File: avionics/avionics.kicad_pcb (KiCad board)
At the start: 4 copper layers, 103 x 60 mm, 68 parts, among them J1 BAT Balancing leads, J2 BAT, J3 PYRO_0, J4 Servo_0, J5 Servo_1, J6 Servo_2, J7 Servo_3, Q1 AO3400A, Q2 AO3401A, U1 Teensy4.1, U2 BMI088, U3 BMP280, U4 MMC5983MA, U5 TPS548B23VANR, U6 74AHCT125

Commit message: hw: make board smaller, misc hotfixes
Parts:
- removed the Q2 at (118.8, 86.4)
- removed TP10: TP_INT_GYR, TestPoint:TestPoint_Pad_D1.5mm
- removed TP11: TP_MAG_INT, TestPoint:TestPoint_Pad_D1.5mm
- removed TP14: TP_5V, TestPoint:TestPoint_Pad_D1.5mm
- removed the TP16 at (174.9, 63.2)
- removed TP17: TP_SERVO_1, TestPoint:TestPoint_Pad_D1.5mm
- removed TP18: TP_SERVO_2, TestPoint:TestPoint_Pad_D1.5mm
- removed TP19: TP_SERVO_3, TestPoint:TestPoint_Pad_D1.5mm
- removed TP2: TP_I2C_SCL, TestPoint:TestPoint_Pad_D1.5mm
- removed TP3: TP_I2C_SDA, TestPoint:TestPoint_Pad_D1.5mm
- removed TP4: TP_MISO, TestPoint:TestPoint_Pad_D1.5mm
- removed TP5: TP_MOSI, TestPoint:TestPoint_Pad_D1.5mm
- removed TP6: TP_SCK, TestPoint:TestPoint_Pad_D1.5mm
- removed TP7: TP_CS_GYR, TestPoint:TestPoint_Pad_D1.5mm
- removed TP8: TP_CS_ACC, TestPoint:TestPoint_Pad_D1.5mm
- removed TP9: TP_INT_ACC, TestPoint:TestPoint_Pad_D1.5mm
- added C1: 100n, Capacitor_SMD:C_0603_1608Metric, F.Cu at (120.2, 60.0)
- added J3: SW_ARM, TerminalBlock_Phoenix:TerminalBlock_Phoenix_MKDS-1,5-2_1x02_P5.00mm_Horizontal, F.Cu at (106.4, 75.8)
- added Q1: RF4C050AP, libraries:TRANS_RF4C_ROM, F.Cu at (135.7, 99.9)
- added R1: 33, Resistor_SMD:R_0603_1608Metric, F.Cu at (146.5, 61.2)
- added R2: 33, Resistor_SMD:R_0603_1608Metric, F.Cu at (143.8, 61.2)
- added R3: 33, Resistor_SMD:R_0603_1608Metric, F.Cu at (141.2, 61.2)
- added SW1: ~{SW_GUIDANCE_EN}, Button_Switch_THT:SW_PUSH_6mm, F.Cu at (150.2, 101.2)
- C10: renamed from C9; footprint Capacitor_SMD:C_0805_2012Metric_Pad1.18x1.45mm_HandSolder -> Capacitor_SMD:C_0603_1608Metric
- C11: renamed from C10; footprint Capacitor_SMD:C_0805_2012Metric_Pad1.18x1.45mm_HandSolder -> Capacitor_SMD:C_0603_1608Metric
- C12: renamed from C11; footprint Capacitor_SMD:C_0805_2012Metric_Pad1.18x1.45mm_HandSolder -> Capacitor_SMD:C_0603_1608Metric
- C13: renamed from C12; footprint Capacitor_SMD:C_0805_2012Metric_Pad1.18x1.45mm_HandSolder -> Capacitor_SMD:C_0603_1608Metric
- C14: renamed from C13; footprint Capacitor_SMD:C_0805_2012Metric_Pad1.18x1.45mm_HandSolder -> Capacitor_SMD:C_0603_1608Metric
- C15: renamed from C14; footprint Capacitor_SMD:C_0805_2012Metric_Pad1.18x1.45mm_HandSolder -> Capacitor_SMD:C_0603_1608Metric
- C16: renamed from C15; footprint Capacitor_SMD:C_0805_2012Metric_Pad1.18x1.45mm_HandSolder -> Capacitor_SMD:C_0603_1608Metric
- C17: renamed from C16; footprint Capacitor_SMD:C_0805_2012Metric_Pad1.18x1.45mm_HandSolder -> Capacitor_SMD:C_0603_1608Metric
- C18: renamed from C17; footprint Capacitor_SMD:C_0805_2012Metric_Pad1.18x1.45mm_HandSolder -> Capacitor_SMD:C_0603_1608Metric
- C2: renamed from C1; footprint Capacitor_SMD:C_0805_2012Metric_Pad1.18x1.45mm_HandSolder -> Capacitor_SMD:C_0603_1608Metric
- C3: renamed from C2; footprint Capacitor_SMD:C_0805_2012Metric_Pad1.18x1.45mm_HandSolder -> Capacitor_SMD:C_0603_1608Metric
- C4: renamed from C3; footprint Capacitor_SMD:C_0805_2012Metric_Pad1.18x1.45mm_HandSolder -> Capacitor_SMD:C_0603_1608Metric
- C5: renamed from C4; footprint Capacitor_SMD:C_0805_2012Metric_Pad1.18x1.45mm_HandSolder -> Capacitor_SMD:C_0603_1608Metric
- C6: renamed from C5; footprint Capacitor_SMD:C_0805_2012Metric_Pad1.18x1.45mm_HandSolder -> Capacitor_SMD:C_0603_1608Metric
- C7: renamed from C6; footprint Capacitor_SMD:C_0805_2012Metric_Pad1.18x1.45mm_HandSolder -> Capacitor_SMD:C_0603_1608Metric
- C8: renamed from C7; footprint Capacitor_SMD:C_0805_2012Metric_Pad1.18x1.45mm_HandSolder -> Capacitor_SMD:C_0603_1608Metric
- C9: renamed from C8; footprint Capacitor_SMD:C_0805_2012Metric_Pad1.18x1.45mm_HandSolder -> Capacitor_SMD:C_0603_1608Metric
- F1: value Littelfuse 1812L090 -> Littelfuse 2920L400
- J1: footprint Connector_JST:JST_XH_S3B-XH-A_1x03_P2.50mm_Horizontal -> Connector_JST:JST_XH_B3B-XH-A_1x03_P2.50mm_Vertical
- L1: value 300n -> 300n (SRP1038A-R33M); footprint Inductor_SMD:L_2512_6332Metric_Pad1.52x3.35mm_HandSolder -> Inductor_SMD:L_Bourns_SRP1038C_10.0x10.0mm
- R10: renamed from R14; footprint Resistor_SMD:R_0805_2012Metric_Pad1.20x1.40mm_HandSolder -> Resistor_SMD:R_0603_1608Metric
- R11: renamed from R7; footprint Resistor_SMD:R_0805_2012Metric_Pad1.20x1.40mm_HandSolder -> Resistor_SMD:R_0603_1608Metric
- R12: renamed from R8; footprint Resistor_SMD:R_0805_2012Metric_Pad1.20x1.40mm_HandSolder -> Resistor_SMD:R_0603_1608Metric
- R13: renamed from R9; footprint Resistor_SMD:R_0805_2012Metric_Pad1.20x1.40mm_HandSolder -> Resistor_SMD:R_0603_1608Metric
- R14: renamed from R10; footprint Resistor_SMD:R_0805_2012Metric_Pad1.20x1.40mm_HandSolder -> Resistor_SMD:R_0603_1608Metric
- R15: renamed from R11; footprint Resistor_SMD:R_0805_2012Metric_Pad1.20x1.40mm_HandSolder -> Resistor_SMD:R_0603_1608Metric
- R16: renamed from R12; footprint Resistor_SMD:R_0805_2012Metric_Pad1.20x1.40mm_HandSolder -> Resistor_SMD:R_0603_1608Metric
- R17: renamed from R13; footprint Resistor_SMD:R_0805_2012Metric_Pad1.20x1.40mm_HandSolder -> Resistor_SMD:R_0603_1608Metric
- R4: renamed from R1; footprint Resistor_SMD:R_0805_2012Metric_Pad1.20x1.40mm_HandSolder -> Resistor_SMD:R_0603_1608Metric
- R5: renamed from R2; footprint Resistor_SMD:R_0805_2012Metric_Pad1.20x1.40mm_HandSolder -> Resistor_SMD:R_0603_1608Metric
- R6: renamed from R3; footprint Resistor_SMD:R_0805_2012Metric_Pad1.20x1.40mm_HandSolder -> Resistor_SMD:R_0603_1608Metric
- R7: renamed from R4; footprint Resistor_SMD:R_0805_2012Metric_Pad1.20x1.40mm_HandSolder -> Resistor_SMD:R_0603_1608Metric
- R8: renamed from R5; footprint Resistor_SMD:R_0805_2012Metric_Pad1.20x1.40mm_HandSolder -> Resistor_SMD:R_0603_1608Metric
- R9: renamed from R6; footprint Resistor_SMD:R_0805_2012Metric_Pad1.20x1.40mm_HandSolder -> Resistor_SMD:R_0603_1608Metric
- U2: footprint BMI088:PQFN50P450X300X100-16N -> libraries:PQFN50P450X300X100-16N
- moved U4 79.9 mm to (171.6, 91.6), turned to 90 degrees
- moved C8 75.9 mm to (171.9, 88.3), turned to 180 degrees
- moved U2 75.4 mm to (172.4, 80.2), turned to 180 degrees
- moved C6 73.2 mm to (172.3, 94.6), turned to 0 degrees
- moved C2 72.9 mm to (172.2, 83.2), turned to 180 degrees
- moved J6 71.0 mm to (123.1, 49.2), turned to 180 degrees
- moved C7 70.6 mm to (168.6, 89.6), turned to 90 degrees
- moved C3 67.4 mm to (171.2, 77.2), turned to 180 degrees
- moved J5 64.3 mm to (106.6, 59.4), turned to -90 degrees
- moved U3 58.4 mm to (162.8, 90.6), turned to -90 degrees
- moved R4 51.8 mm to (159.5, 76.5), turned to 180 degrees
- moved R5 51.3 mm to (156.5, 77.2), turned to 90 degrees
- moved C4 50.2 mm to (160.0, 89.0), turned to -90 degrees
- moved C5 49.4 mm to (160.0, 92.2), turned to -90 degrees
- moved J7 45.2 mm to (139.9, 49.2)
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- renumbered J3 to J4, J4 to J5, J5 to J6, J6 to J7, J7 to J8, Q1 to Q2, TP20 to TP16
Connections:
- J4 pad 1: +BATT -> Net-(J3-Pin_2)
- U1 pad 12: /IMU/CS_ACC -> Net-(U1-10_CS_MQSR)
- U1 pad 13: /IMU/MOSI -> Net-(U1-11_MOSI_CTX1)
- U1 pad 14: /IMU/MISO -> Net-(U1-12_MISO_MQSL)
- U1 pad 22: unconnected-(U1-30_CRX3-Pad22) -> Net-(U1-30_CRX3)
- U1 pad 32: /PSU/BAT_CELL_1 -> /PSU/BAT_CELL_0
- U1 pad 33: /PSU/BAT_CELL_0 -> /PSU/BAT_CELL_1
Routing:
- net +5V: track 127.3 -> 24.0 mm, vias 8 -> 23
- net /Barometer/SDA: track 123.0 -> 33.3 mm, vias 1 -> 0
- net /IMU/MOSI: track 122.4 -> 37.6 mm
- net +BATT: track 65.2 -> 1.50 mm, vias 3 -> 29
- net Net-(U1-30_CRX3): track 0.00 -> 60.4 mm
- net /Magnetometer/INT: track 79.2 -> 28.5 mm
- net /IMU/CS_ACC: track 84.6 -> 37.9 mm
- net GND: track 125.8 -> 82.9 mm, vias 23 -> 171
- net Net-(U5-CFG1): track 52.8 -> 13.3 mm, vias 0 -> 2
- net /Pyro_and_servos/PYRO_0: track 60.2 -> 99.2 mm, vias 0 -> 4
- net /IMU/MISO: track 81.5 -> 42.6 mm
- net +3.3V: track 77.9 -> 41.5 mm, vias 3 -> 7
- net SPI_SCK: track 68.7 -> 36.1 mm
- net Net-(J7-Pin_3): track 17.8 -> 39.0 mm, vias 0 -> 1
- net Net-(C15-Pad1): track 21.0 -> 0.00 mm
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- added copper zone on F.Cu, net +5V
- added copper zone on F.Cu, net +BATT
- added copper zone on In2.Cu, net +BATT
- added copper zone on B.Cu, net GND
- added copper zone on F.Cu, net GND
- added copper zone on F.Cu, net Net-(C15-Pad1)
- added copper zone on F.Cu, net Net-(C17-Pad2)
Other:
- board size 103 x 60 mm -> 76 x 60 mm

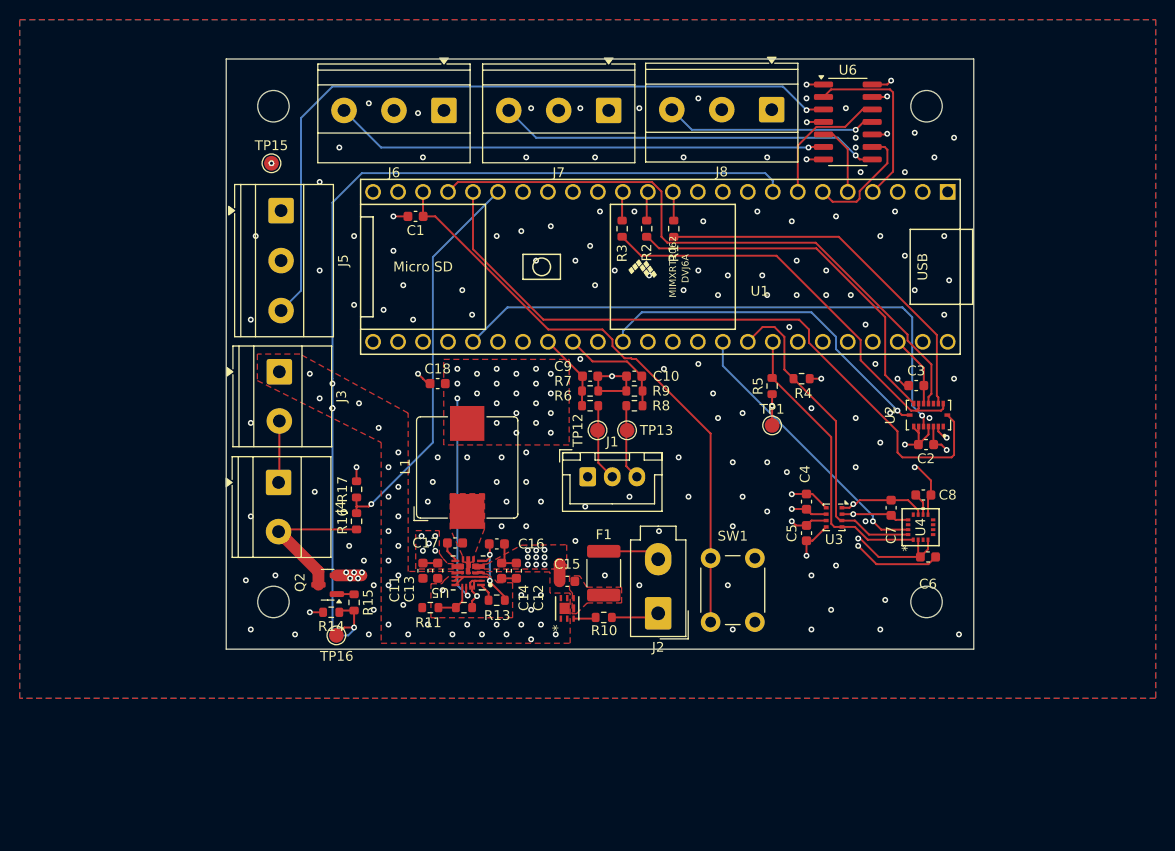
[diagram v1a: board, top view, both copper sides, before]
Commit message: added labels
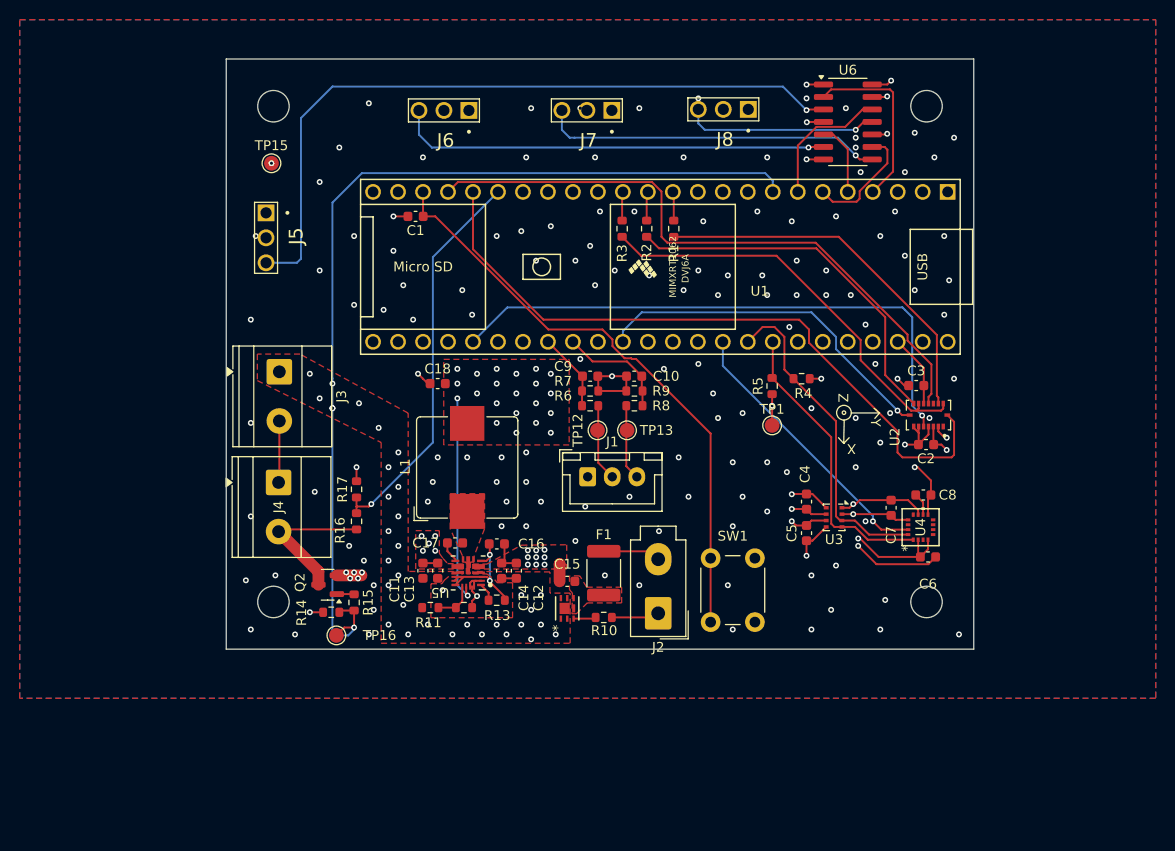
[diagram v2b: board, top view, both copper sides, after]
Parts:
- J5, J6, J7, J8: footprint TerminalBlock_Phoenix:TerminalBlock_Phoenix_MKDS-1,5-3-5.08_1x03_P5.08mm_Horizontal -> 5-146290-3:TE_5-146290-3
- moved J8 4.92 mm to (151.5, 49.1)
- moved J5 3.16 mm to (105.0, 62.2)
- moved J7 2.22 mm to (137.7, 49.2)
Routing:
- net Net-(J6-Pin_3): track 50.3 -> 44.2 mm
- net Net-(J7-Pin_3): track 39.0 -> 34.8 mm
- net Net-(J5-Pin_3): track 75.9 -> 73.5 mm
- net Net-(J8-Pin_3): track 21.6 -> 19.7 mm
- net GND: vias 171 -> 170
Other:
- board text added: "Project Viikate V1"
- board text added: "X"
- board text added: "Y"
- board text added: "Z"

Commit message: hw: order pcb
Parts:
- removed TP12: TP_VBAT_0, TestPoint:TestPoint_Pad_D1.5mm
- removed TP13: TP_VBAT_1, TestPoint:TestPoint_Pad_D1.5mm
- removed TP15: TP_GND, TestPoint:TestPoint_Pad_D1.5mm
- removed TP16: TP_PYRO_0, TestPoint:TestPoint_Pad_D1.5mm
- added C19: 1000u, Capacitor_THT:CP_Radial_D10.0mm_P5.00mm, F.Cu at (153.8, 105.5)
- added D1: SMF10A, Diode_SMD:D_SMF, F.Cu at (107.8, 109.5)
- added D2: CPDH5V0U, Diode_SMD:D_SOD-523, F.Cu at (122.3, 61.7)
- added D3: CPDH5V0U, Diode_SMD:D_SOD-523, F.Cu at (112.0, 62.5)
- added D4: CPDUR5V0-HF, Diode_SMD:D_0603_1608Metric, F.Cu at (122.5, 64.1)
- added D5: CPDUR5V0-HF, Diode_SMD:D_0603_1608Metric, F.Cu at (111.8, 65.0)
- added D6: CPDUR5V0-HF, Diode_SMD:D_0603_1608Metric, F.Cu at (122.5, 67.5)
- added D7: CPDUR5V0-HF, Diode_SMD:D_0603_1608Metric, F.Cu at (111.8, 67.5)
- added J9: Conn_01x04_Pin, Connector_PinHeader_2.54mm:PinHeader_1x04_P2.54mm_Vertical, F.Cu at (115.2, 70.1)
- added M3: MountingHole_3.2mm_M3, MountingHole:MountingHole_3.2mm_M3, F.Cu at (104.8, 64.8)
- added R18: 100k, Resistor_SMD:R_0603_1608Metric, F.Cu at (132.8, 106.6)
- added R19: 33, Resistor_SMD:R_0603_1608Metric, F.Cu at (131.1, 106.6)
- added R20: 56k, Resistor_SMD:R_0603_1608Metric, F.Cu at (120.3, 99.2)
- added R21: 33k, Resistor_SMD:R_0603_1608Metric, F.Cu at (121.9, 99.2)
- added REF**: MountingHole_3.2mm_M3, MountingHole:MountingHole_3.2mm_M3, F.Cu at (171.2, 115.2)
- added REF**: MountingHole_3.2mm_M3, MountingHole:MountingHole_3.2mm_M3, F.Cu at (171.2, 64.8)
- added REF**: MountingHole_3.2mm_M3, MountingHole:MountingHole_3.2mm_M3, F.Cu at (104.8, 115.2)
- added TP2: TP_GND, TestPoint:TestPoint_Pad_D1.5mm, F.Cu at (134.0, 63.0)
- C10: value 100n -> 22u; footprint Capacitor_SMD:C_0603_1608Metric -> Capacitor_SMD:C_1210_3225Metric
- C11: footprint Capacitor_SMD:C_0603_1608Metric -> Capacitor_SMD:C_1210_3225Metric
- C12: value 22u -> 1u
- C14, C16: value 1u -> 100n
- C15: value 100n -> 1u
- C17: value 100n -> 47u; footprint Capacitor_SMD:C_0603_1608Metric -> Capacitor_SMD:C_1210_3225Metric
- C18: value 47u -> 1u
- F1: footprint Fuse:Fuse_1812_4532Metric_Pad1.30x3.40mm_HandSolder -> Fuse:Fuse_2920_7451Metric
- J1: value BAT Balancing leads -> XT60M; footprint Connector_JST:JST_XH_B3B-XH-A_1x03_P2.50mm_Vertical -> Connector_AMASS:AMASS_XT60-M_1x02_P7.20mm_Vertical
- J2: value BAT -> 1x2_header; footprint Connector_Molex:Molex_Mini-Fit_Jr_5566-02A_2x01_P4.20mm_Vertical -> TerminalBlock_Phoenix:TerminalBlock_Phoenix_MKDS-1,5-2_1x02_P5.00mm_Horizontal
- J3: value SW_ARM -> 1x2_header
- J4: value PYRO_0 -> 1x3_header; footprint TerminalBlock_Phoenix:TerminalBlock_Phoenix_MKDS-1,5-2_1x02_P5.00mm_Horizontal -> Connector_PinHeader_2.54mm:PinHeader_1x03_P2.54mm_Vertical
- J5: value Servo_0 -> 1x3_header; footprint 5-146290-3:TE_5-146290-3 -> Connector_PinHeader_2.54mm:PinHeader_1x03_P2.54mm_Vertical
- J6: value Servo_1 -> 1x3_header; footprint 5-146290-3:TE_5-146290-3 -> Connector_PinHeader_2.54mm:PinHeader_1x03_P2.54mm_Vertical
- J7: value Servo_2 -> 1x3_header; footprint 5-146290-3:TE_5-146290-3 -> Connector_PinHeader_2.54mm:PinHeader_1x03_P2.54mm_Vertical
- J8: value Servo_3 -> Conn_01x04_Pin; footprint 5-146290-3:TE_5-146290-3 -> Connector_PinHeader_2.54mm:PinHeader_1x04_P2.54mm_Vertical
- L1: value 300n (SRP1038A-R33M) -> 300n
- R10: value 47k -> 2.7k
- R11: value 37.4k -> 100k
- R12: value 10k -> 56k
- R13: value 10k -> 33k
- R14: value 100k -> 47k
- R15: value 100 -> 37.4k
- R16: value 56k -> 10k
- R17: value 33k -> 10k
- R4, R5: value 2.7k -> 33
- R6: value 10k -> 33
- R7: value 25k -> 2.7k
- R8: value 56k -> 2.7k
- R9: value 33k -> 2.7k
- SW1: value ~{SW_GUIDANCE_EN} -> 6x6mm Switch
- U2: value BMI088 -> ISM330DHCX; footprint libraries:PQFN50P450X300X100-16N -> Package_LGA:LGA-14_3x2.5mm_P0.5mm_LayoutBorder3x4y
- U3: value BMP280 -> BME280; footprint Package_LGA:Bosch_LGA-8_2x2.5mm_P0.65mm_ClockwisePinNumbering -> Package_LGA:Bosch_LGA-8_2.5x2.5mm_P0.65mm_ClockwisePinNumbering
- moved J6 78.3 mm to (160.5, 118.0)
- moved J5 76.9 mm to (158.0, 118.0), turned to 180 degrees
- moved J7 73.3 mm to (163.0, 118.0)
- moved J4 58.1 mm to (155.4, 118.0), turned to 180 degrees
- moved U6 52.4 mm to (165.8, 102.8)
- moved C2 47.2 mm to (127.2, 68.8), turned to 90 degrees
- moved R5 47.0 mm to (110.0, 70.3)
- moved C18 44.5 mm to (148.3, 113.2), turned to 0 degrees
- moved U2 43.5 mm to (129.9, 70.9)
- moved J3 43.0 mm to (124.7, 114.8), turned to 0 degrees
- moved C3 40.9 mm to (131.2, 68.5)
- moved J8 38.7 mm to (119.0, 70.1)
- moved J1 37.4 mm to (104.4, 103.5)
- moved R10 36.0 mm to (122.5, 69.0), turned to 180 degrees
- moved J2 34.6 mm to (113.5, 114.8), turned to 0 degrees
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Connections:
- net Net-(U1-30_CRX3) renamed /SW_GUIDANCE
- C10 pad 1: /PSU/BAT_CELL_1 -> +BATT
- C14 pad 1: +BATT -> Net-(C14-Pad1)
- C15 pad 1: Net-(C15-Pad1) -> Net-(U5-CFG1)
- C16 pad 1: Net-(U5-CFG1) -> Net-(U5-BST)
- C16 pad 2: GND -> Net-(C16-Pad2)
- C17 pad 1: Net-(U5-BST) -> +5V
- C17 pad 2: Net-(C17-Pad2) -> GND
- C3 pad 1: +3.3V -> GND
- C3 pad 2: GND -> +3.3V
- C9 pad 1: /PSU/BAT_CELL_0 -> /BAT_VOLTAGE
- F1 pad 1: Net-(J2-Pin_2) -> /PSU/BAT_CONN+
- F1 pad 2: Net-(C15-Pad1) -> Net-(C14-Pad1)
- J1 pad 2: Net-(J1-Pin_2) -> /PSU/BAT_CONN+
- J2 pad 1: GND -> +BATT
- J2 pad 2: Net-(J2-Pin_2) -> /Pyro_and_servos/ARM_Vout
- J3 pad 1: +BATT -> /Pyro_and_servos/ARM_Vout
- J3 pad 2: Net-(J3-Pin_2) -> /Pyro_and_servos/PYRO_0_Vout
- J4 pad 1: Net-(J3-Pin_2) -> GND
- J4 pad 2: Net-(J4-Pin_2) -> +5V
- J5 pad 3: Net-(J5-Pin_3) -> /Pyro_and_servos/SERVO_1
- J6 pad 3: Net-(J6-Pin_3) -> /Pyro_and_servos/SERVO_2
- J7 pad 3: Net-(J7-Pin_3) -> /Pyro_and_servos/SERVO_3
- J8 pad 2: +5V -> /I2C_OUT_SDA
- J8 pad 3: Net-(J8-Pin_3) -> /I2C_OUT_SCL
- L1 pad 1: Net-(C17-Pad2) -> Net-(C16-Pad2)
- Q1 pad 4: Net-(C15-Pad1) -> Net-(C14-Pad1)
- Q1 pad 8: Net-(C15-Pad1) -> Net-(C14-Pad1)
- Q2 pad 1: Net-(Q2-G) -> /Pyro_and_servos/PYRO_0_GATE
- Q2 pad 3: Net-(J4-Pin_2) -> /Pyro_and_servos/PYRO_0_Vout
- R1 pad 1: /IMU/CS_ACC -> /SPI_CS
- R10 pad 1: Net-(Q1-Pad3) -> +3.3V
- R10 pad 2: GND -> /I2C_OUT_SDA
- R11 pad 1: +BATT -> /SPI_CS
- R11 pad 2: Net-(U5-EN) -> GND
- R12 pad 1: Net-(U5-EN) -> +BATT
- R12 pad 2: GND -> /BAT_VOLTAGE
- R13 pad 1: Net-(U5-PG) -> /BAT_VOLTAGE
- R13 pad 2: Net-(U5-CFG1) -> GND
- R14 pad 1: /Pyro_and_servos/PYRO_0 -> Net-(Q1-Pad3)
- R15 pad 1: Net-(Q2-G) -> +BATT
- R15 pad 2: /Pyro_and_servos/PYRO_0 -> Net-(U5-EN)
- R16 pad 1: Net-(J4-Pin_2) -> Net-(U5-EN)
- R16 pad 2: /Pyro_and_servos/PYRO_0_CONT -> GND
- R17 pad 1: /Pyro_and_servos/PYRO_0_CONT -> Net-(U5-PG)
- R17 pad 2: GND -> Net-(U5-CFG1)
- R2 pad 1: /IMU/MOSI -> /SPI_MOSI
- R3 pad 1: /IMU/MISO -> /SPI_MISO
- R4 pad 1: +3.3V -> Net-(U1-13_SCK_LED)
- R4 pad 2: /Barometer/SDA -> /SPI_SCK
- R5 pad 1: +3.3V -> Net-(U1-35_TX8)
- R5 pad 2: /Barometer/SCL -> /UART_TX
- R6 pad 1: Net-(J1-Pin_2) -> Net-(U1-34_RX8)
- R6 pad 2: /PSU/BAT_CELL_0 -> /UART_RX
- R7 pad 1: /PSU/BAT_CELL_0 -> +3.3V
- R7 pad 2: GND -> /I2C_SDA
- R8 pad 1: Net-(J1-Pin_3) -> +3.3V
- R8 pad 2: /PSU/BAT_CELL_1 -> /I2C_SCL
- R9 pad 1: /PSU/BAT_CELL_1 -> +3.3V
- R9 pad 2: GND -> /I2C_OUT_SCL
- U1 pad 15: +3.3V -> unconnected-(U1-3V3-Pad15)
- U1 pad 16: unconnected-(U1-24_A10_TX6_SCL2-Pad16) -> /I2C_OUT_SCL
- U1 pad 17: unconnected-(U1-25_A11_RX6_SDA2-Pad17) -> /I2C_OUT_SDA
- U1 pad 19: /Pyro_and_servos/PYRO_0_CONT -> /PYRO_0_CONT
- U1 pad 20: /IMU/INT_ACC -> /INT_ACC
- U1 pad 21: /IMU/INT_GYR -> /INT_GYR
- U1 pad 26: unconnected-(U1-34_RX8-Pad26) -> Net-(U1-34_RX8)
- U1 pad 27: unconnected-(U1-35_TX8-Pad27) -> Net-(U1-35_TX8)
- U1 pad 29: IMU_CS_GYR -> unconnected-(U1-37_CS-Pad29)
- U1 pad 32: /PSU/BAT_CELL_0 -> unconnected-(U1-40_A16-Pad32)
- U1 pad 33: /PSU/BAT_CELL_1 -> /BAT_VOLTAGE
- U1 pad 35: SPI_SCK -> Net-(U1-13_SCK_LED)
- U1 pad 4: /Pyro_and_servos/SERVO_0_PWM -> /SERVO_3_PWM
- U1 pad 40: /Barometer/SDA -> /I2C_SDA
- U1 pad 41: /Barometer/SCL -> /I2C_SCL
- U1 pad 5: /Pyro_and_servos/SERVO_1_PWM -> /SERVO_2_PWM
- U1 pad 6: /Pyro_and_servos/SERVO_2_PWM -> /SERVO_1_PWM
- U1 pad 7: /Pyro_and_servos/SERVO_3_PWM -> /SERVO_0_PWM
- U1 pad 8: /Pyro_and_servos/PYRO_0 -> /PYRO_0
- U2 pad 1: unconnected-(U2-INT2-Pad1) -> /SPI_MISO
- U2 pad 10: /IMU/MISO -> unconnected-(U2-OCS_AUX-Pad10)
- U2 pad 11: +3.3V -> unconnected-(U2-SDO_AUX-Pad11)
- U2 pad 12: /IMU/INT_GYR -> /SPI_CS
- U2 pad 13: unconnected-(U2-INT4-Pad13) -> /SPI_SCK
- U2 pad 14: /IMU/CS_ACC -> /SPI_MOSI
- U2 pad 3: +3.3V -> GND
- U2 pad 4: GND -> /INT_ACC
- U2 pad 5: IMU_CS_GYR -> +3.3V
- U2 pad 8: SPI_SCK -> +3.3V
- U2 pad 9: /IMU/MOSI -> /INT_GYR
- U3 pad 3: /Barometer/SDA -> /I2C_SDA
- U3 pad 4: /Barometer/SCL -> /I2C_SCL
- U4 pad 1: /Barometer/SCL -> /I2C_SCL
- U4 pad 16: /Barometer/SDA -> /I2C_SDA
- U5 pad 7: Net-(C17-Pad2) -> Net-(C16-Pad2)
- U5 pad 8: Net-(C17-Pad2) -> Net-(C16-Pad2)
- U5 pad 9: Net-(C17-Pad2) -> Net-(C16-Pad2)
- U6 pad 11: Net-(J8-Pin_3) -> /Pyro_and_servos/SERVO_3
- U6 pad 12: /Pyro_and_servos/SERVO_3_PWM -> /SERVO_3_PWM
- U6 pad 2: /Pyro_and_servos/SERVO_0_PWM -> /SERVO_0_PWM
- U6 pad 3: Net-(J5-Pin_3) -> /Pyro_and_servos/SERVO_0
- U6 pad 5: /Pyro_and_servos/SERVO_1_PWM -> /SERVO_1_PWM
- U6 pad 6: Net-(J6-Pin_3) -> /Pyro_and_servos/SERVO_1
- U6 pad 8: Net-(J7-Pin_3) -> /Pyro_and_servos/SERVO_2
- U6 pad 9: /Pyro_and_servos/SERVO_2_PWM -> /SERVO_2_PWM
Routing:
- net /Pyro_and_servos/PYRO_0: track 99.2 -> 0.00 mm, vias 4 -> 0
- net Net-(J5-Pin_3): track 73.5 -> 0.00 mm, vias 1 -> 0
- net /IMU/INT_ACC: track 70.0 -> 0.00 mm
- net /IMU/INT_GYR: track 64.4 -> 0.00 mm
- net IMU_CS_GYR: track 58.1 -> 0.00 mm, vias 1 -> 0
- net /I2C_SDA: track 0.00 -> 54.8 mm
- net /I2C_SCL: track 0.00 -> 54.3 mm
- net Net-(J6-Pin_3): track 44.2 -> 0.00 mm, vias 1 -> 0
- net /IMU/MISO: track 42.6 -> 0.00 mm
- net /Pyro_and_servos/PYRO_0_CONT: track 40.3 -> 0.00 mm, vias 1 -> 0
- net /PYRO_0: track 0.00 -> 39.8 mm, vias 0 -> 1
- net /IMU/CS_ACC: track 37.9 -> 0.00 mm
- net /IMU/MOSI: track 37.6 -> 0.00 mm
- net SPI_SCK: track 36.1 -> 0.00 mm, vias 1 -> 0
- net GND: track 82.9 -> 117.7 mm, vias 170 -> 174
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- added copper zone on F.Cu, net Net-(C14-Pad1)
- added copper zone on F.Cu, net Net-(C16-Pad2)
- removed copper zone on F.Cu, net Net-(C15-Pad1)
- removed copper zone on F.Cu, net Net-(C17-Pad2)
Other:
- outline, holes or cut-outs redrawn
- board text added: "S0"
- board text added: "S1"
- board text added: "S2"
- board text added: "S3"
